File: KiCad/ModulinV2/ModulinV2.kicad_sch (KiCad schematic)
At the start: 11 parts, among them IC1 TL074HIDR, J1 NRJ4HF-1

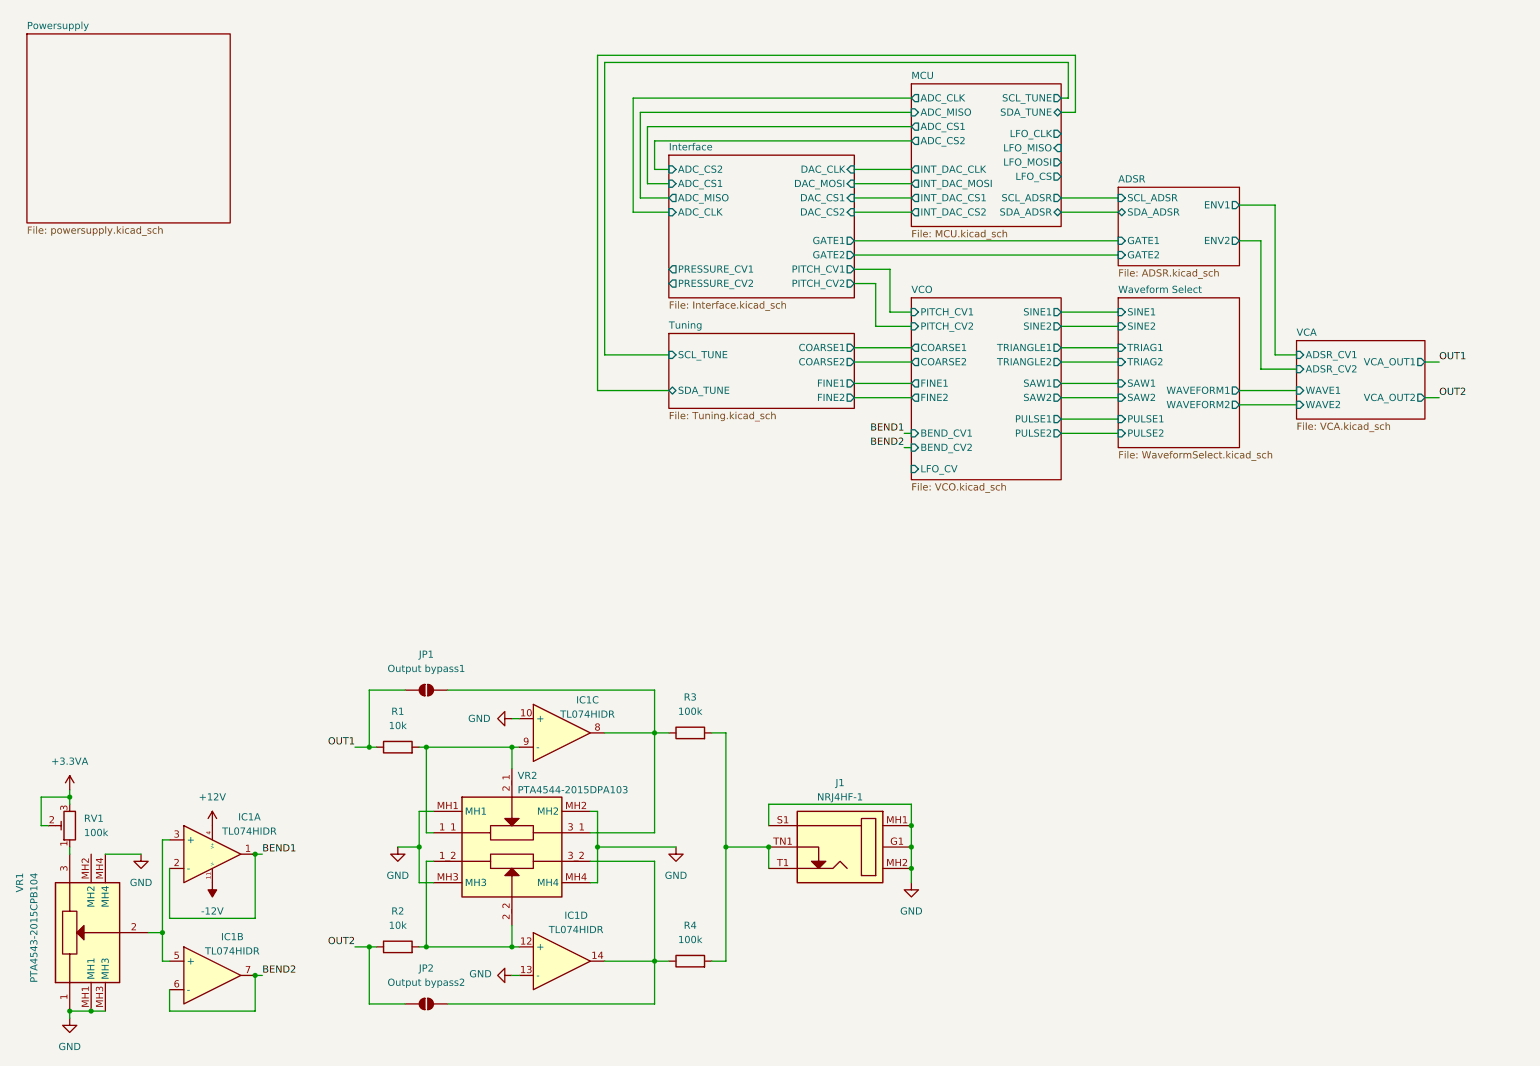
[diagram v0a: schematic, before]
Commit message: Designed the schmitt triger (finally)
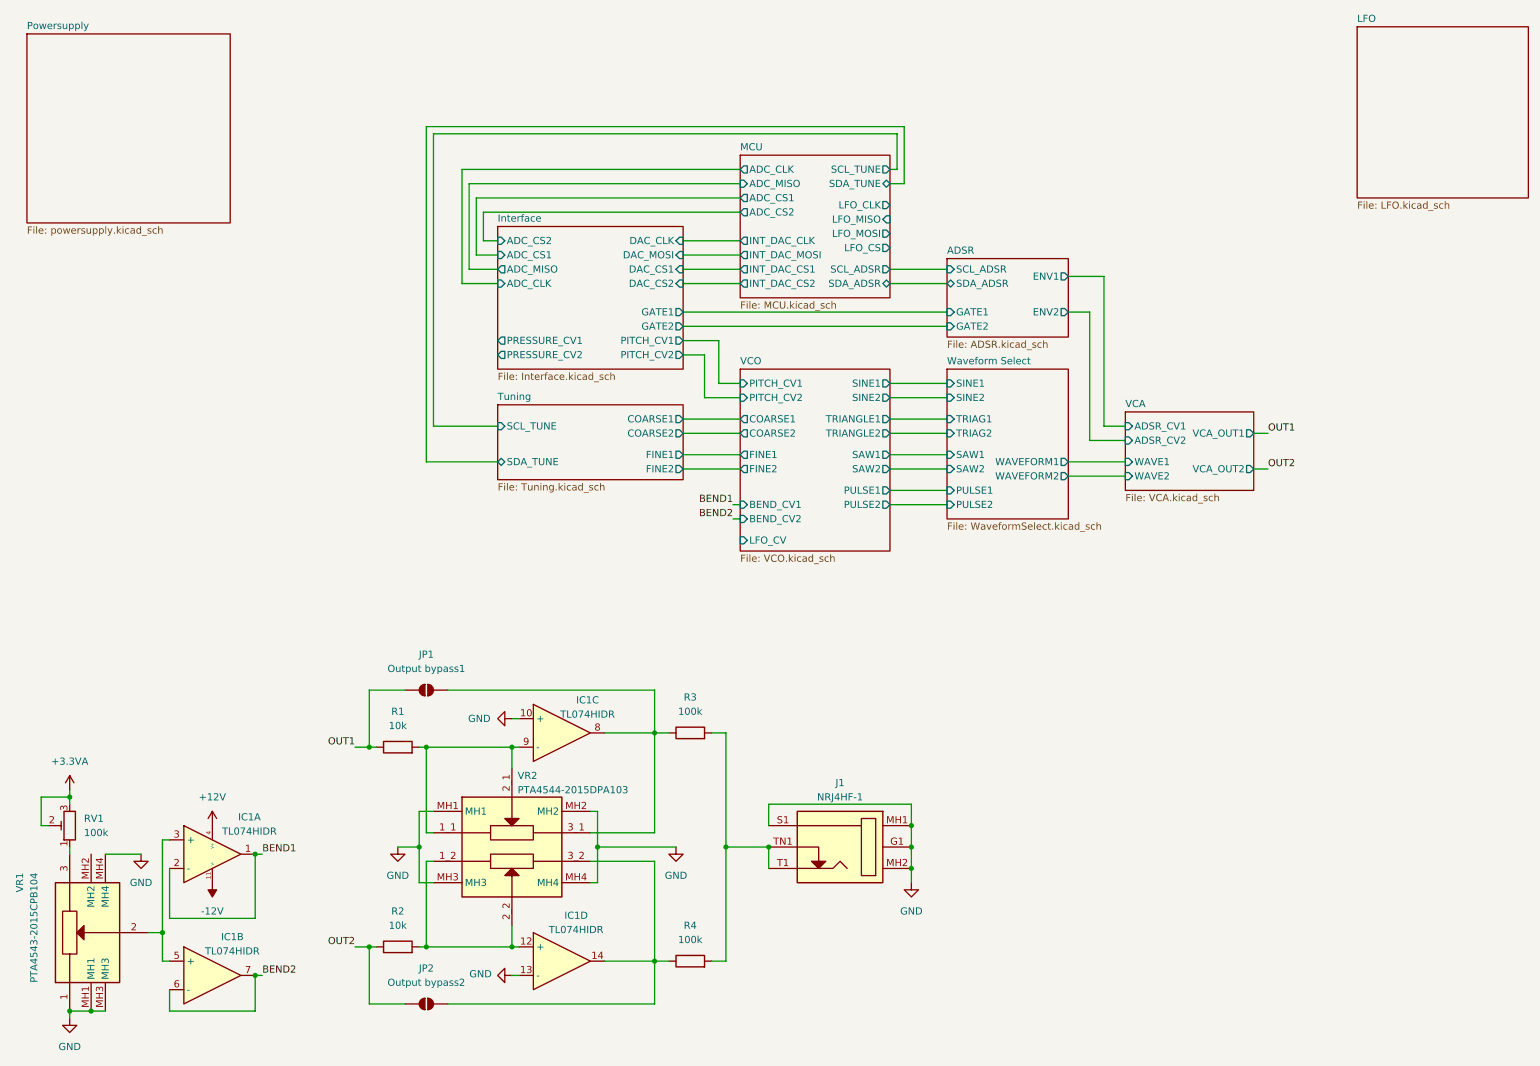
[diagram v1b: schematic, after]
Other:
- added sheet LFO (LFO.kicad_sch)

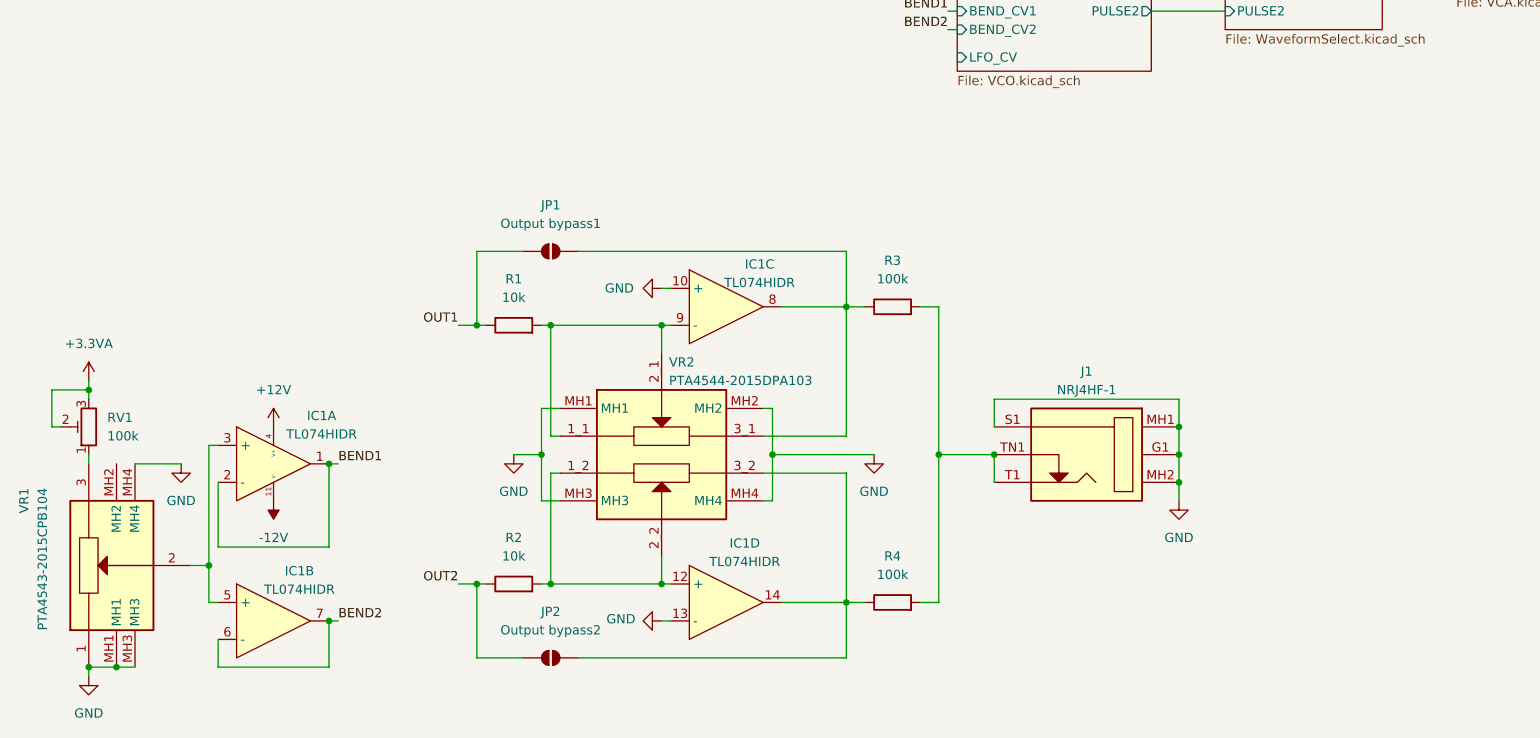
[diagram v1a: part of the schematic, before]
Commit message: Started adding footprints for capacitors
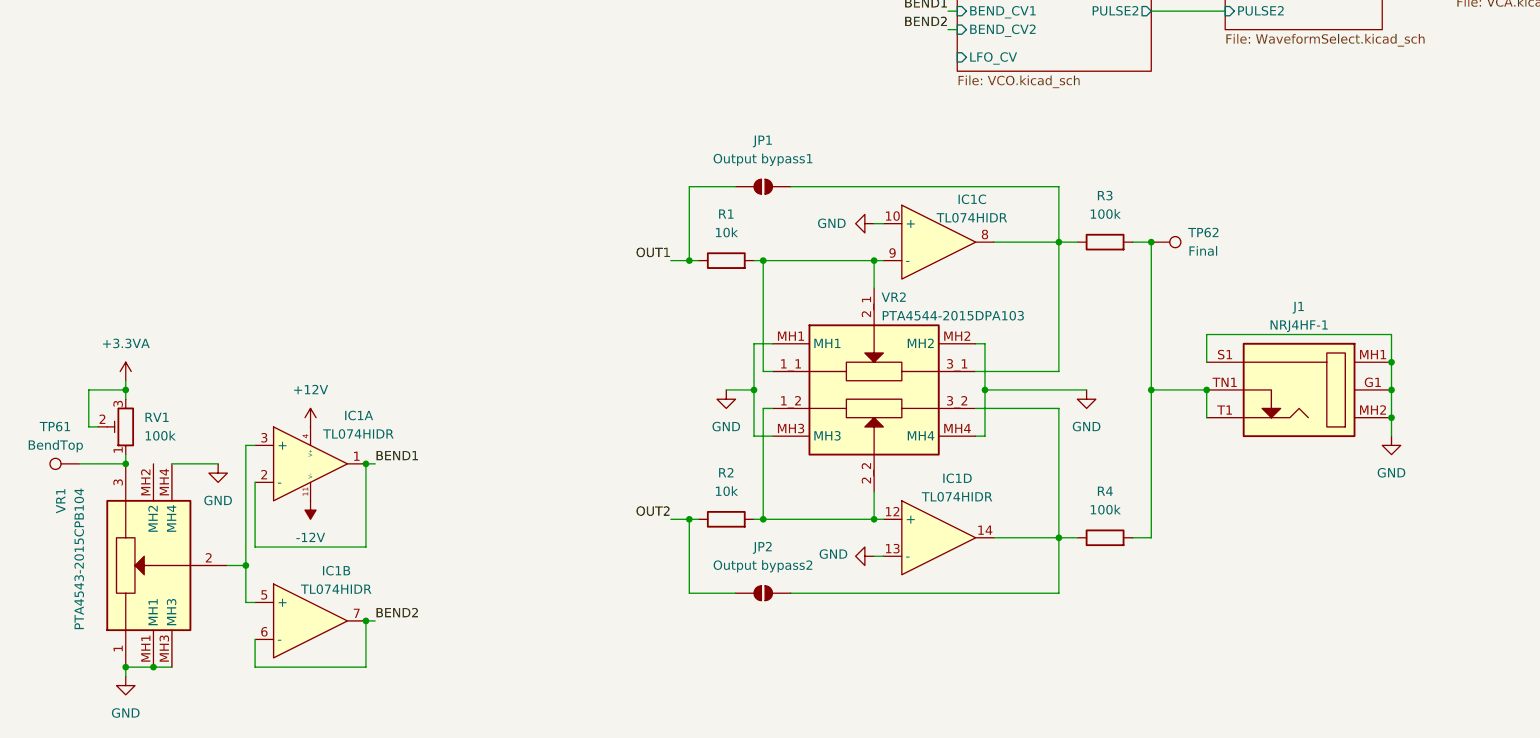
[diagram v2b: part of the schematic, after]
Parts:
- added TP61: BendTop, SamacSys_Parts:TestPointLoop, symbol Connector:TestPoint
- added TP62: Final, SamacSys_Parts:TestPointLoop, symbol Connector:TestPoint
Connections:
- net at RV1.1, VR1.3: now also TP61.1
- net at J1.T1, J1.TN1, R3.2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: now also TP62.1
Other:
- moved on the sheet: IC1A, IC1B, IC1C, IC1D, J1, JP1, JP2, R1, R2, R3, R4, RV1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

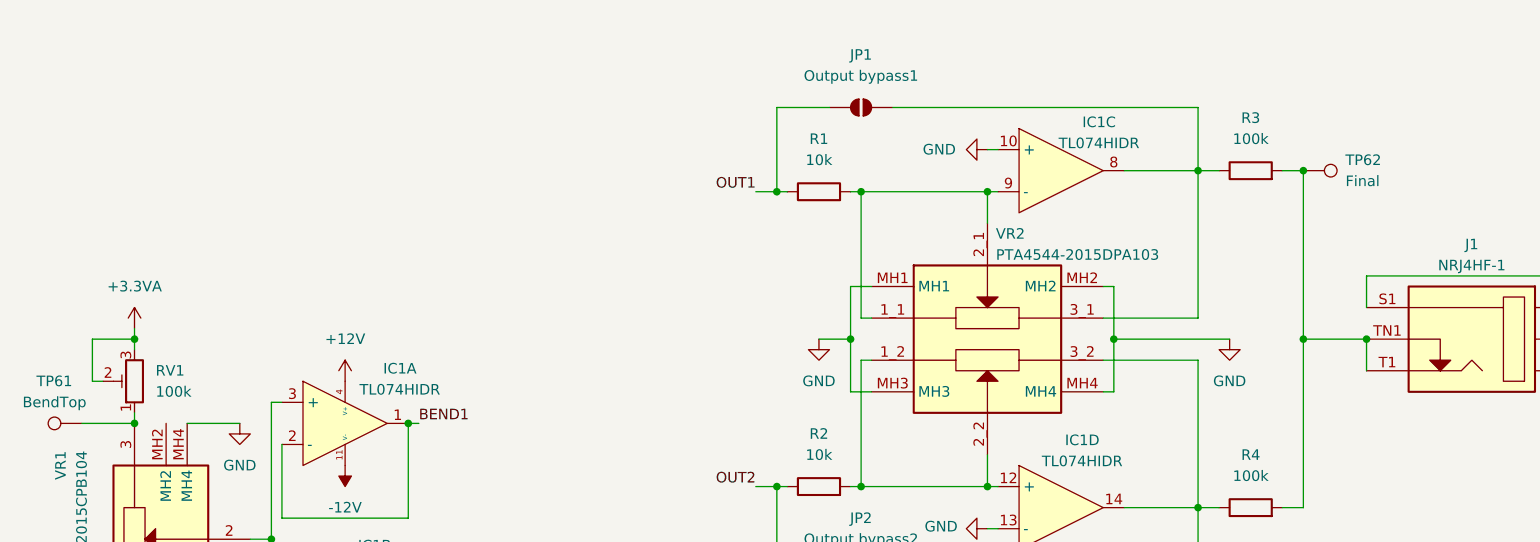
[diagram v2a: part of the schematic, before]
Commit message: Added footprints to all capacitors and potentiometers
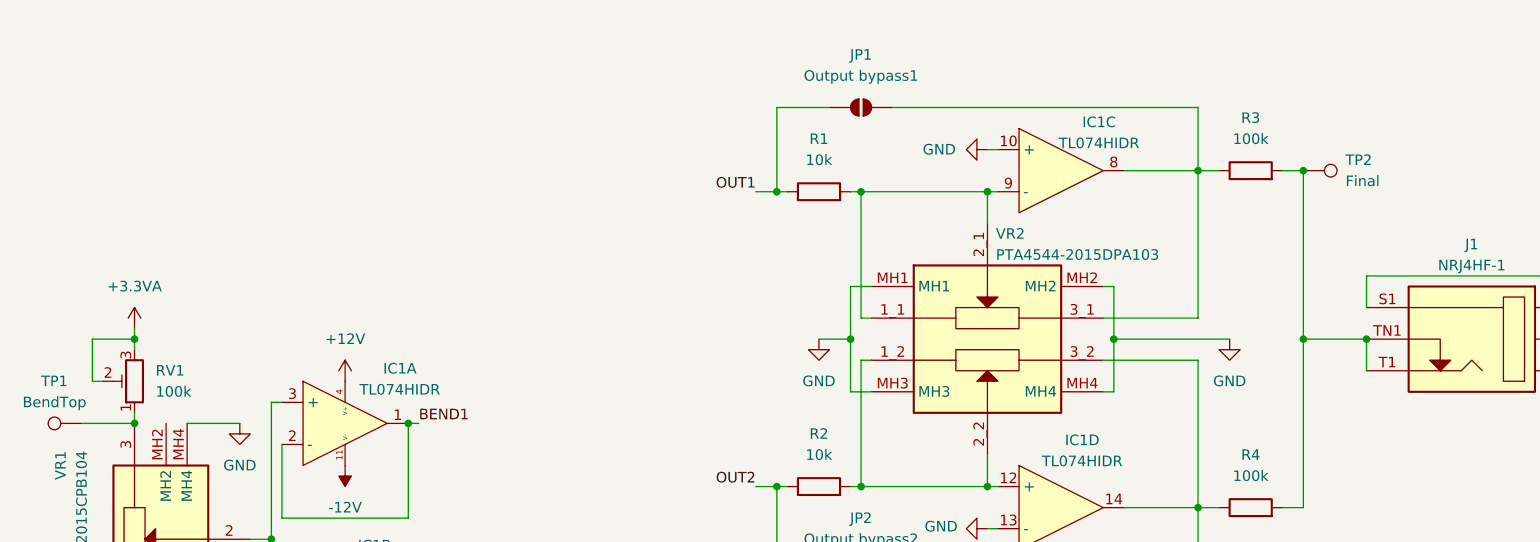
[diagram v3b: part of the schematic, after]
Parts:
- RV1: footprint (none) -> SamacSys_Parts:PV36W201C01B00
- renumbered TP61 to TP1, TP62 to TP2
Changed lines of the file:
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@@
 			)
 		)
-		(property "Footprint" ""
+		(property "Footprint" "SamacSys_Parts:PV36W201C01B00"
 			(at 27.94 156.21 0)
 			(effects
@@
 		(dnp no)
 		(fields_autoplaced yes)
-		(property "Reference" "TP62"
+		(property "Reference" "TP2"
 			(at 173.99 129.5399 90)
 			(effects
@@
 			(project "ModulinV2"
 				(path "/c6b34a57-3941-4b56-8b80-1848c7f41082"
-					(reference "TP62")
+					(reference "TP2")
 					(unit 1)
 				)
@@
 		(dnp no)
 		(fields_autoplaced yes)
-		(property "Reference" "TP61"
+		(property "Reference" "TP1"
 			(at 18.288 156.21 90)
 			(effects
@@
 			(project "ModulinV2"
 				(path "/c6b34a57-3941-4b56-8b80-1848c7f41082"
-					(reference "TP61")
-					(unit 1)
-				)
+					(reference "TP1")
+					(unit 1)
+				)
